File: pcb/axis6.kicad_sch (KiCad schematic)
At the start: 10 parts, among them J16 Mini v1.0 FEMALE sockets, J26 MOTOR PHASES male 1x3, J36 ENCODER JST-SH 6p, J46 MINI POWER: +12V / GND

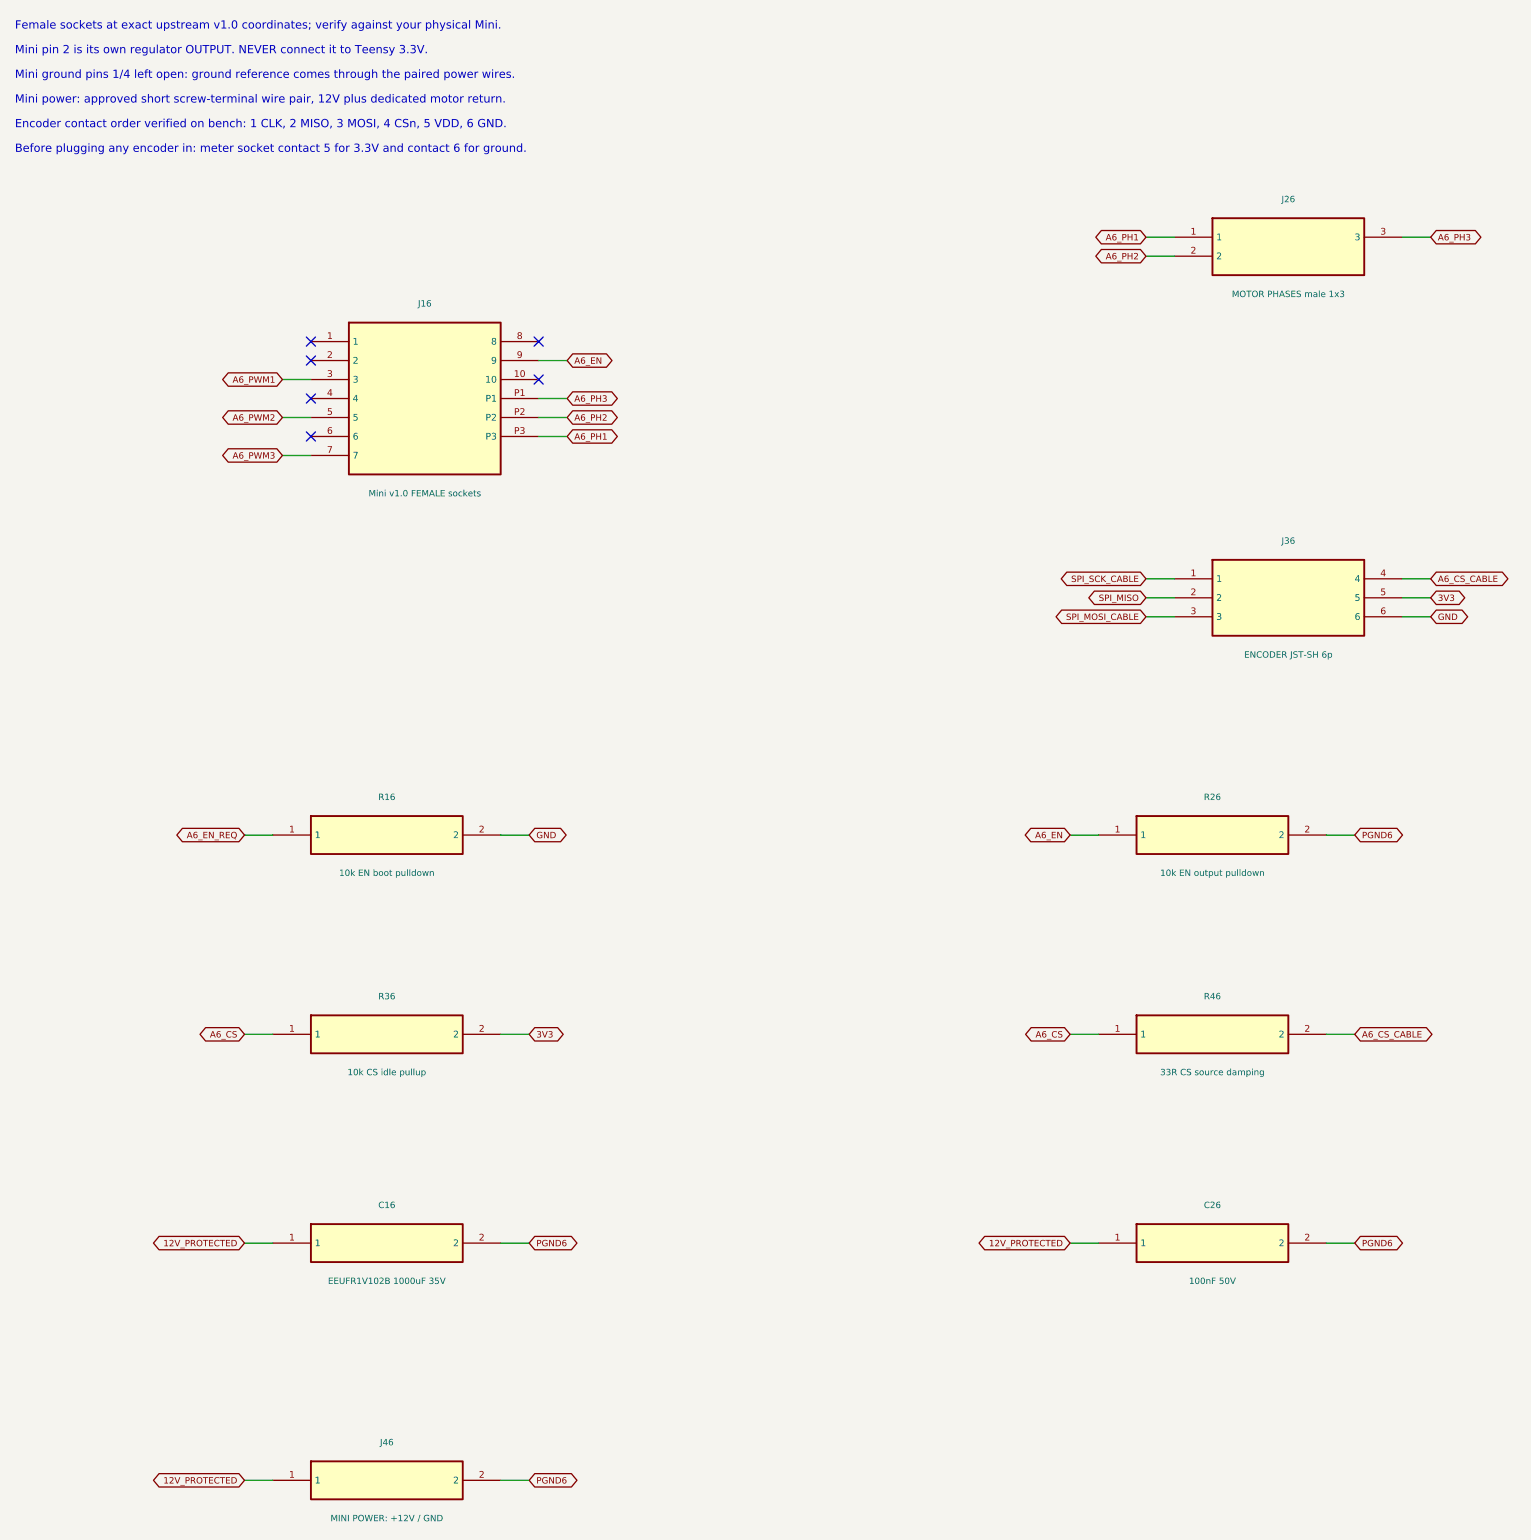
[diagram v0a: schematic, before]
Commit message: feat: finish through-hole six-axis carrier review design
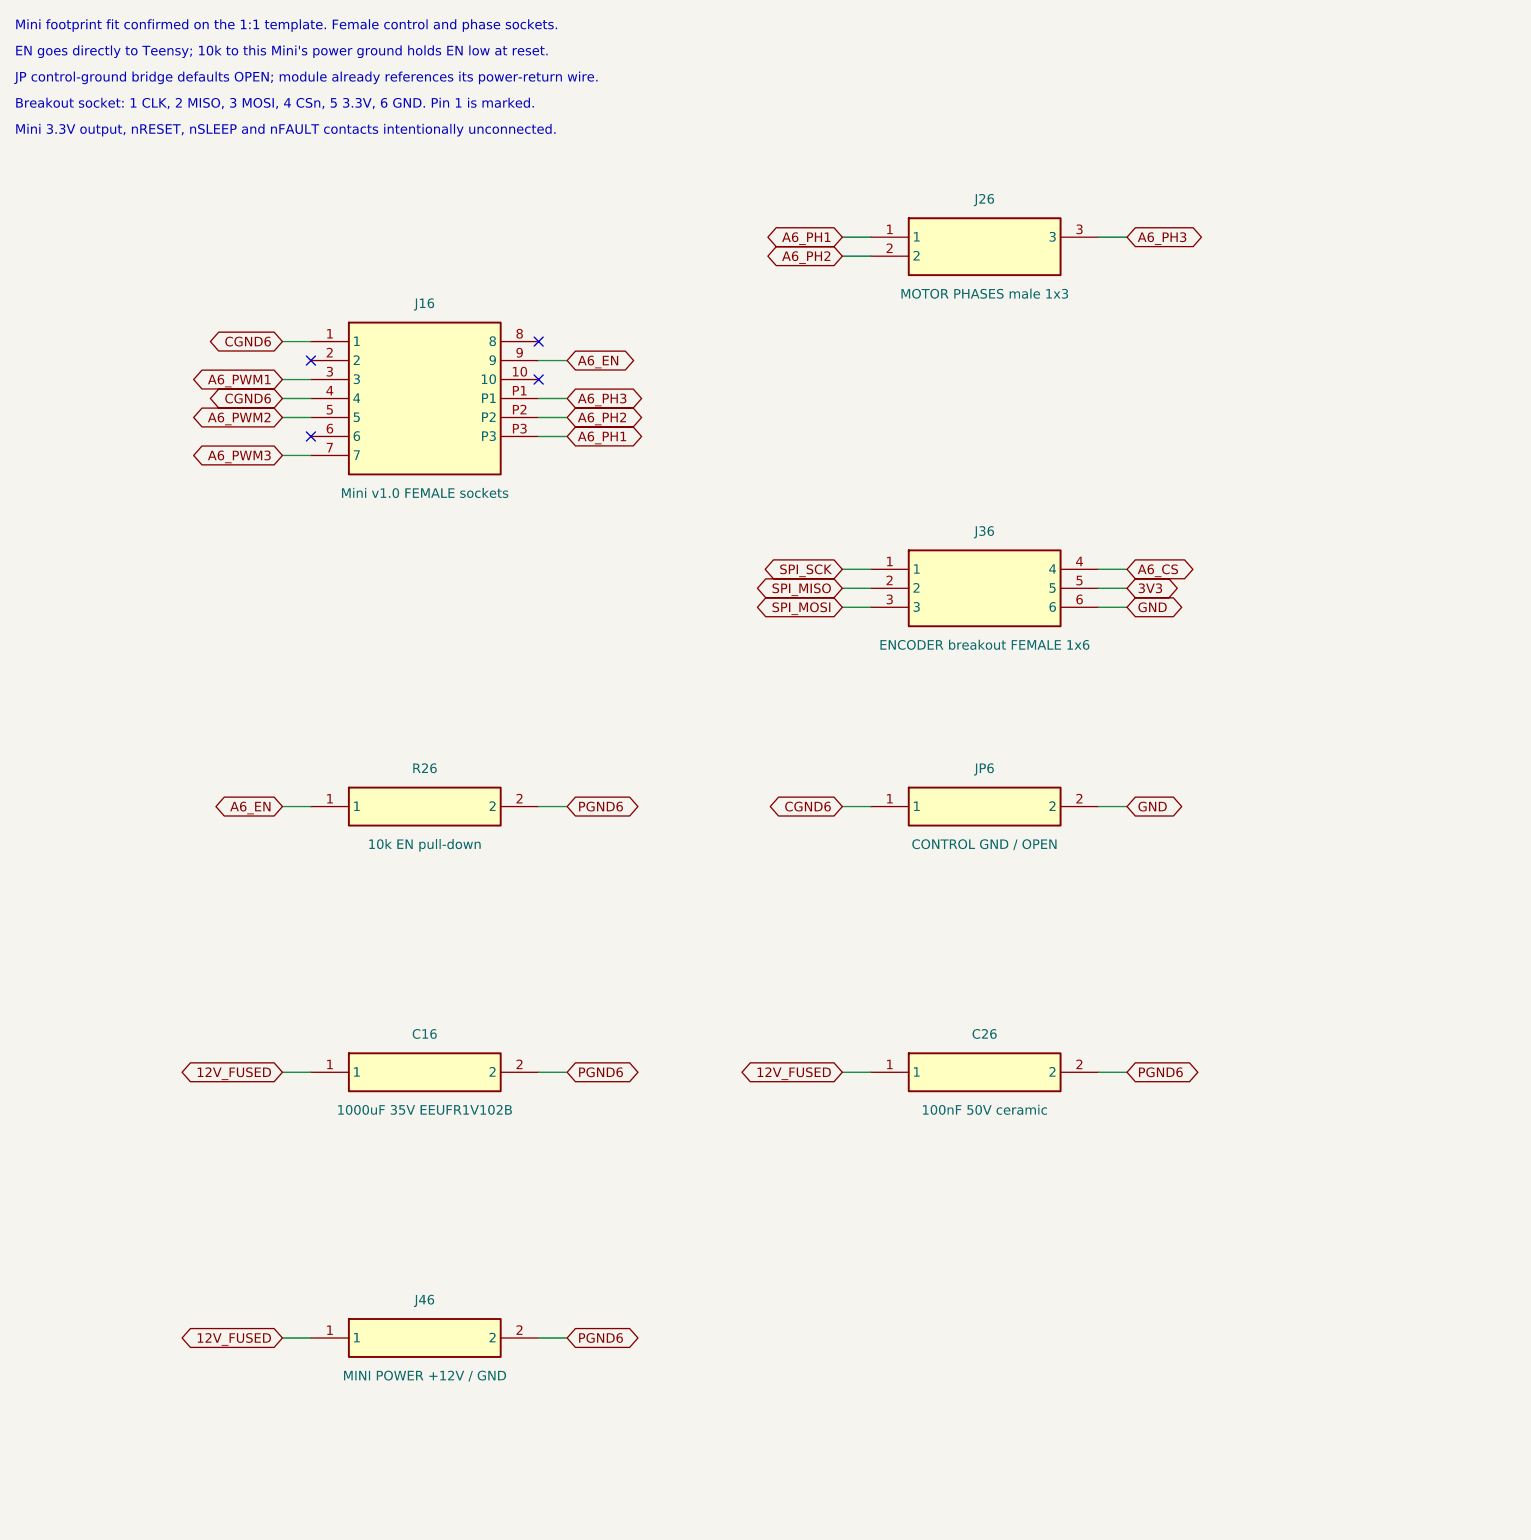
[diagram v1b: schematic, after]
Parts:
- removed R16: 10k EN boot pulldown, Resistor_SMD:R_0603_1608Metric, symbol TrueSkate:R16
- removed R36: 10k CS idle pullup, Resistor_SMD:R_0603_1608Metric, symbol TrueSkate:R36
- removed R46: 33R CS source damping, Resistor_SMD:R_0603_1608Metric, symbol TrueSkate:R46
- added JP6: CONTROL GND / OPEN, TrueSkate:GroundBridge_THT, symbol TrueSkate:JP6
- C16: value EEUFR1V102B 1000uF 35V -> 1000uF 35V EEUFR1V102B; LCSC C128476 -> (none)
- C26: value 100nF 50V -> 100nF 50V ceramic; footprint Capacitor_SMD:C_0603_1608Metric -> Capacitor_THT:C_Disc_D5.0mm_W2.5mm_P5.00mm; LCSC C14663 -> (none)
- J36: value ENCODER JST-SH 6p -> ENCODER breakout FEMALE 1x6; footprint Connector_JST:JST_SH_BM06B-SRSS-TB_1x06-1MP_P1.00mm_Vertical -> Connector_PinSocket_2.54mm:PinSocket_1x06_P2.54mm_Vertical; LCSC C160392 -> (none)
- J46: value MINI POWER: +12V / GND -> MINI POWER +12V / GND
- R26: value 10k EN output pulldown -> 10k EN pull-down; footprint Resistor_SMD:R_0603_1608Metric -> Resistor_THT:R_Axial_DIN0207_L6.3mm_D2.5mm_P7.62mm_Horizontal; LCSC C25804 -> (none)
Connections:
- net A6_CS_CABLE is gone; now on net A6_CS: J36.4
- net GND: now also JP6.2
- net CGND6: now reaches J16.1
- net CGND6: now also J16.4, JP6.1
- net 12V_PROTECTED renamed 12V_FUSED
- net SPI_MOSI_CABLE renamed SPI_MOSI
- net SPI_SCK_CABLE renamed SPI_SCK
- no-connect marks 6 -> 4
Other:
- note added: "Breakout socket: 1 CLK, 2 MISO, 3 MOSI, 4 CSn, 5 3.3V, 6 GND. Pin 1 is marked."
- note added: "EN goes directly to Teensy; 10k to this Mini's power ground holds EN low at reset."
- note added: "JP control-ground bridge defaults OPEN; module already references its power-return wire."
- note added: "Mini 3.3V output, nRESET, nSLEEP and nFAULT contacts intentionally unconnected."
- note added: "Mini footprint fit confirmed on the 1:1 template. Female control and phase sockets."
- note removed: "Before plugging any encoder in: meter socket contact 5 for 3.3V and contact 6 for ground."
- note removed: "Encoder contact order verified on bench: 1 CLK, 2 MISO, 3 MOSI, 4 CSn, 5 VDD, 6 GND."
- note removed: "Female sockets at exact upstream v1.0 coordinates; verify against your physical Mini."
- note removed: "Mini ground pins 1/4 left open: ground reference comes through the paired power wires."
- note removed: "Mini pin 2 is its own regulator OUTPUT. NEVER connect it to Teensy 3.3V."
- note removed: "Mini power: approved short screw-terminal wire pair, 12V plus dedicated motor return."
- title: 08 / Axis 6: middle_splay -> 07 / A6: middle_splay
- moved on the sheet: C16, C26, J26, J36, J46, R26

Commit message: feat: use exact Mini v1.0 footprints with direct power routing
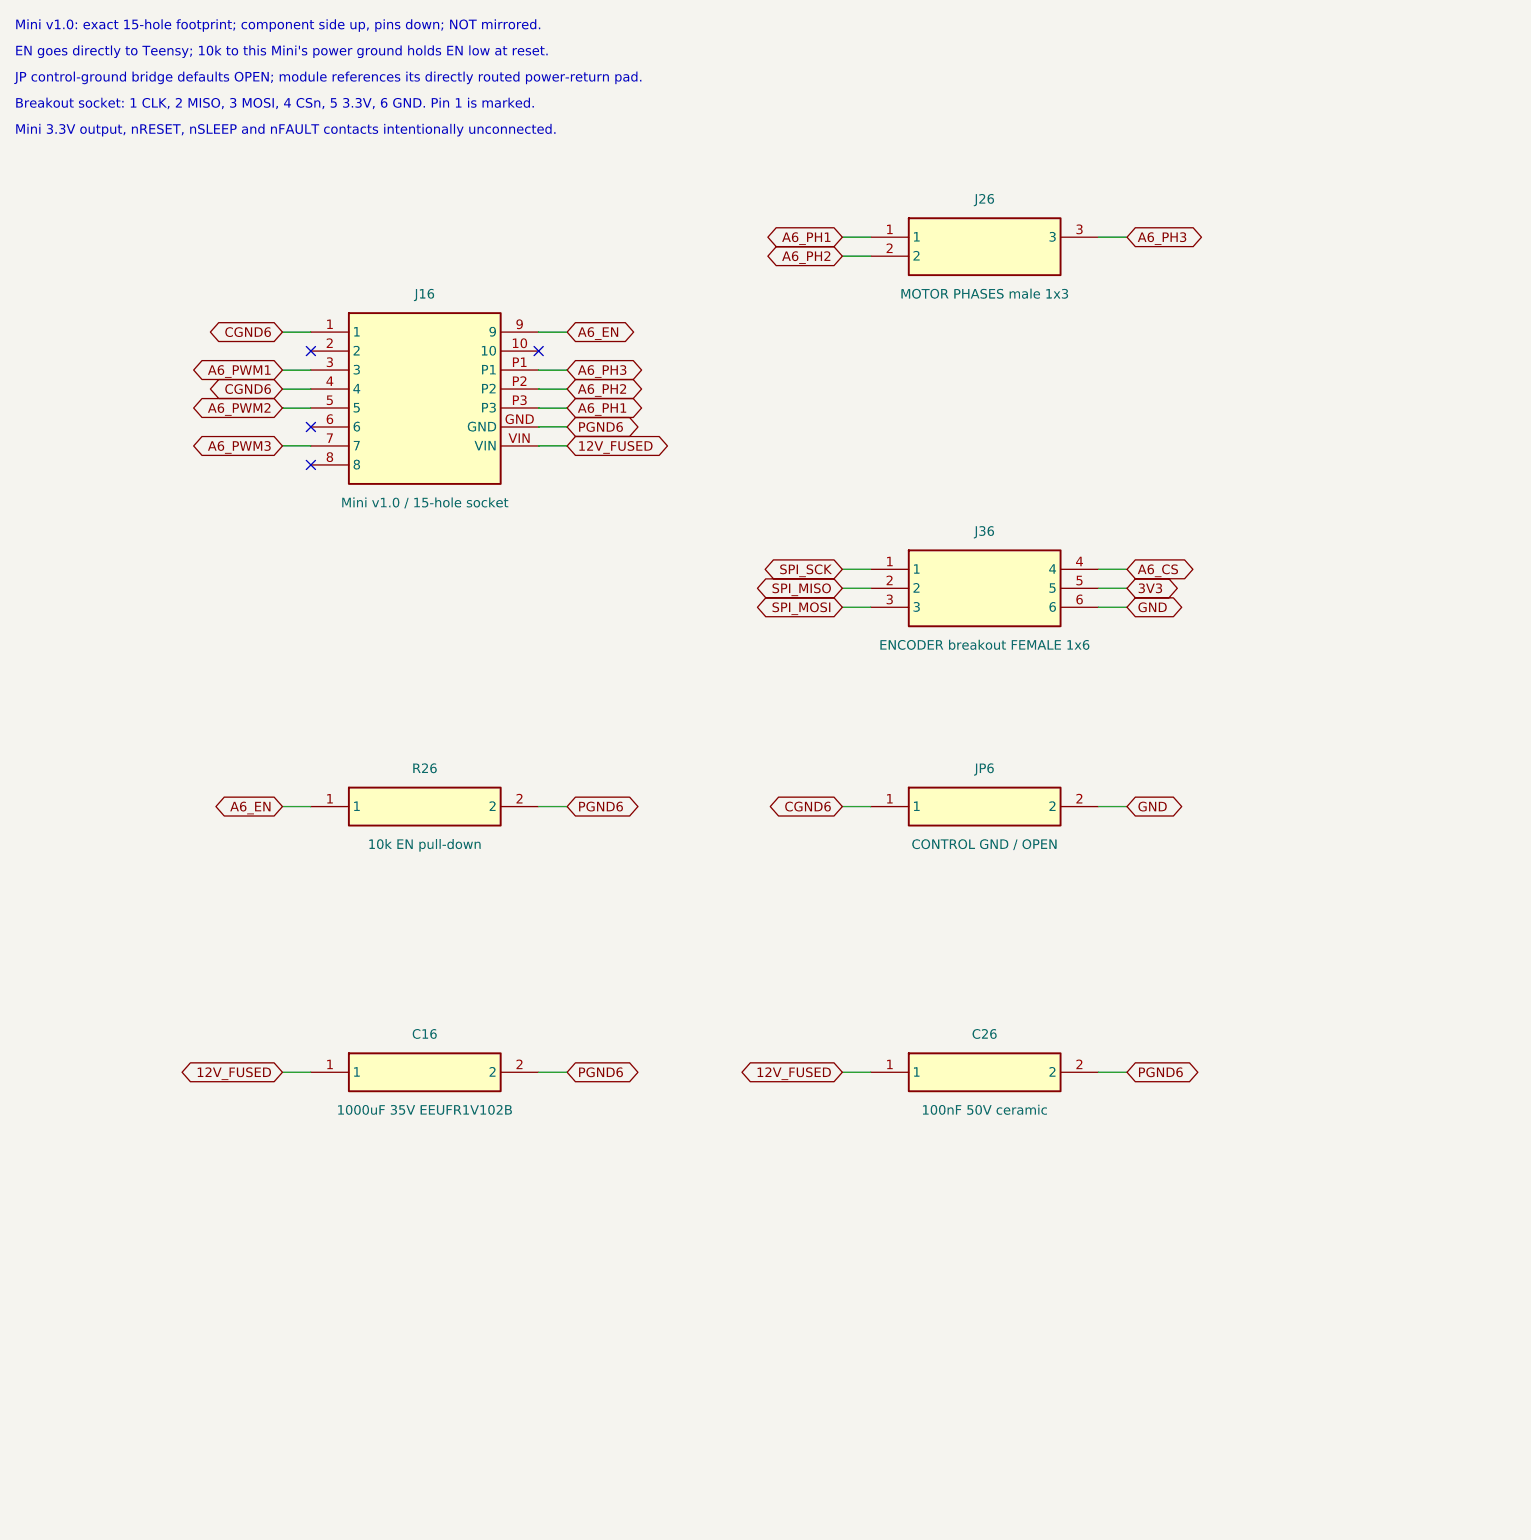
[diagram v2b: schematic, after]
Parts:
- removed J46: MINI POWER +12V / GND, TerminalBlock_Phoenix:TerminalBlock_Phoenix_MKDS-1-2-3.81_1x02_P3.81mm_Horizontal, symbol TrueSkate:J46
- J16: value Mini v1.0 FEMALE sockets -> Mini v1.0 / 15-hole socket; footprint TrueSkate:Mini_v1_Sockets -> TrueSkate:SimpleFOC_Mini_v1.0
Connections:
- net 12V_FUSED: now also J16.VIN
- net PGND6: now also J16.GND
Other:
- note added: "JP control-ground bridge defaults OPEN; module references its directly routed power-return pad."
- note added: "Mini v1.0: exact 15-hole footprint; component side up, pins down; NOT mirrored."
- note removed: "JP control-ground bridge defaults OPEN; module already references its power-return wire."
- note removed: "Mini footprint fit confirmed on the 1:1 template. Female control and phase sockets."
